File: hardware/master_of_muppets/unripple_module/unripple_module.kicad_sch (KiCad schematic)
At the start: 2 parts

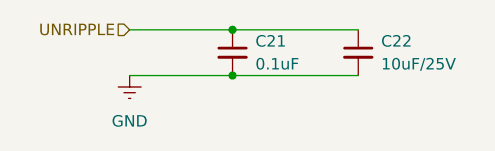
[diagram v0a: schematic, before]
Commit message: Making the boards truly hierarchical using projectinstances plugin
https://github.com/OfficialDyray/projectinstances
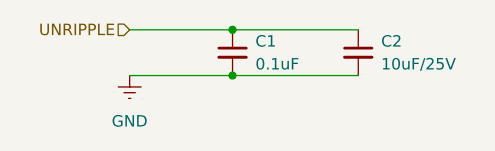
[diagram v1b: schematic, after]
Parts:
- renumbered C21 to C1, C22 to C2
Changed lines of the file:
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@@
 		(dnp no)
 		(fields_autoplaced yes)
-		(property "Reference" "C22"
+		(property "Reference" "C2"
 			(at 106.68 66.0462 0)
 			(effects
@@
 				(path "/01709e3c-d295-4eba-a9f6-77b38e73bd4a/60709206-8158-4f80-9acc-4f76df38190b/415bd524-e348-40cf-853f-c7af6379b92b/eef141d8-f350-40f2-990d-9c18dcf6372d"
 					(reference "C36")
+					(unit 1)
+				)
+			)
+			(project "amp_module"
+				(path "/187e3c00-5c30-42c2-89ec-585912782641/45d11efb-a1cc-46e8-9e3b-dcea3e8724d6"
+					(reference "C4")
+					(unit 1)
+				)
+				(path "/187e3c00-5c30-42c2-89ec-585912782641/eef141d8-f350-40f2-990d-9c18dcf6372d"
+					(reference "C2")
+					(unit 1)
+				)
+			)
+			(project "unripple_module"
+				(path "/5d7da71d-c580-4c32-9092-b7aa9321dacb"
+					(reference "C2")
 					(unit 1)
 				)
@@
 		(dnp no)
 		(fields_autoplaced yes)
-		(property "Reference" "#PWR055"
+		(property "Reference" "#PWR0111"
 			(at 78.74 76.2 0)
 			(effects
@@
 				(path "/01709e3c-d295-4eba-a9f6-77b38e73bd4a/60709206-8158-4f80-9acc-4f76df38190b/415bd524-e348-40cf-853f-c7af6379b92b/eef141d8-f350-40f2-990d-9c18dcf6372d"
 					(reference "#PWR062")
+					(unit 1)
+				)
+			)
+			(project "amp_module"
+				(path "/187e3c00-5c30-42c2-89ec-585912782641/45d11efb-a1cc-46e8-9e3b-dcea3e8724d6"
+					(reference "#PWR0112")
+					(unit 1)
+				)
+				(path "/187e3c00-5c30-42c2-89ec-585912782641/eef141d8-f350-40f2-990d-9c18dcf6372d"
+					(reference "#PWR0111")
+					(unit 1)
+				)
+			)
+			(project "unripple_module"
+				(path "/5d7da71d-c580-4c32-9092-b7aa9321dacb"
+					(reference "#PWR01")
 					(unit 1)
 				)
@@
 		(dnp no)
 		(fields_autoplaced yes)
-		(property "Reference" "C21"
+		(property "Reference" "C1"
 			(at 92.71 66.0462 0)
 			(effects
@@
 				)
 			)
+			(project "amp_module"
+				(path "/187e3c00-5c30-42c2-89ec-585912782641/45d11efb-a1cc-46e8-9e3b-dcea3e8724d6"
+					(reference "C3")
+					(unit 1)
+				)
+				(path "/187e3c00-5c30-42c2-89ec-585912782641/eef141d8-f350-40f2-990d-9c18dcf6372d"
+					(reference "C1")
+					(unit 1)
+				)
+			)
+			(project "unripple_module"
+				(path "/5d7da71d-c580-4c32-9092-b7aa9321dacb"
+					(reference "C1")
+					(unit 1)
+				)
+			)
 		)
 	)
+	(sheet_instances
+		(path "/"
+			(page "1")
+		)
+	)
+	(embedded_fonts no)
 )
